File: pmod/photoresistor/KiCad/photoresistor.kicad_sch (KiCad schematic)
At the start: 4 parts, among them J2 Conn_01x06_Pin

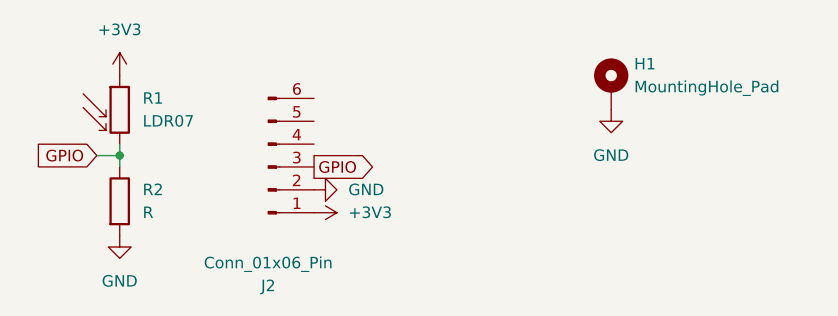
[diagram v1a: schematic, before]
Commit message: docs: add images, fix docs
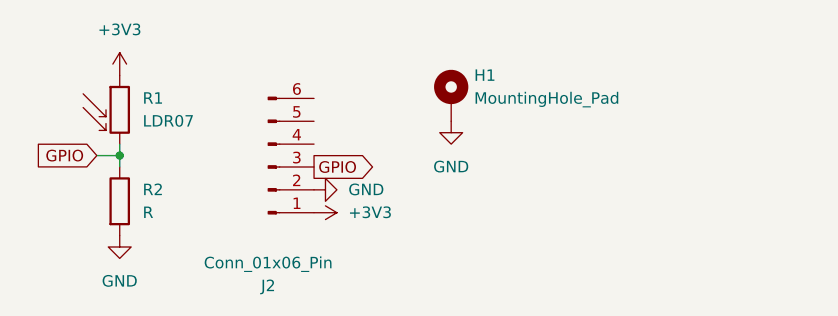
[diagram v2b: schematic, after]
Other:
- moved on the sheet: H1
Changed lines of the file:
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@@
 	(symbol
 		(lib_id "power:GND")
-		(at 133.35 71.12 0)
+		(at 115.57 72.39 0)
 		(unit 1)
 		(body_style 1)
@@
 		(fields_autoplaced yes)
 		(property "Reference" "#PWR05"
-			(at 133.35 77.47 0)
+			(at 115.57 78.74 0)
 			(hide yes)
 			(show_name no)
@@
 		)
 		(property "Value" "GND"
-			(at 133.35 76.2 0)
+			(at 115.57 77.47 0)
 			(show_name no)
 			(do_not_autoplace no)
@@
 		)
 		(property "Footprint" ""
-			(at 133.35 71.12 0)
+			(at 115.57 72.39 0)
 			(hide yes)
 			(show_name no)
@@
 		)
 		(property "Datasheet" ""
-			(at 133.35 71.12 0)
+			(at 115.57 72.39 0)
 			(hide yes)
 			(show_name no)
@@
 		)
 		(property "Description" "Power symbol creates a global label with name \"GND\" , ground"
-			(at 133.35 71.12 0)
+			(at 115.57 72.39 0)
 			(hide yes)
 			(show_name no)
@@
 	(symbol
 		(lib_id "Mechanical:MountingHole_Pad")
-		(at 133.35 68.58 0)
+		(at 115.57 69.85 0)
 		(unit 1)
 		(body_style 1)
@@
 		(fields_autoplaced yes)
 		(property "Reference" "H1"
-			(at 135.89 66.0399 0)
+			(at 118.11 67.3099 0)
 			(show_name no)
 			(do_not_autoplace no)
@@
 		)
 		(property "Value" "MountingHole_Pad"
-			(at 135.89 68.5799 0)
+			(at 118.11 69.8499 0)
 			(show_name no)
 			(do_not_autoplace no)
@@
 		)
 		(property "Footprint" ""
-			(at 133.35 68.58 0)
+			(at 115.57 69.85 0)
 			(hide yes)
 			(show_name no)
@@
 		)
 		(property "Datasheet" ""
-			(at 133.35 68.58 0)
+			(at 115.57 69.85 0)
 			(hide yes)
 			(show_name no)
@@
 		)
 		(property "Description" "Mounting Hole with connection"
-			(at 133.35 68.58 0)
-			(hide yes)
-			(show_name no)
+			(at 115.57 69.85 0)
+			(hide yes)
+			(show_name no)
